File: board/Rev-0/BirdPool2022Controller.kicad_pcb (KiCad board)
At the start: 2 copper layers, 69.8 x 50.8 mm, 28 parts, among them J1 ISP, J2 OSTVN02A150, J3 OSTVN04A150, J4 OSTVN02A150, J5 OSTVN04A150, J6 Conn_01x06, K1 G5LE-14_DC5, U1 PC817, U2 PIC18F1330

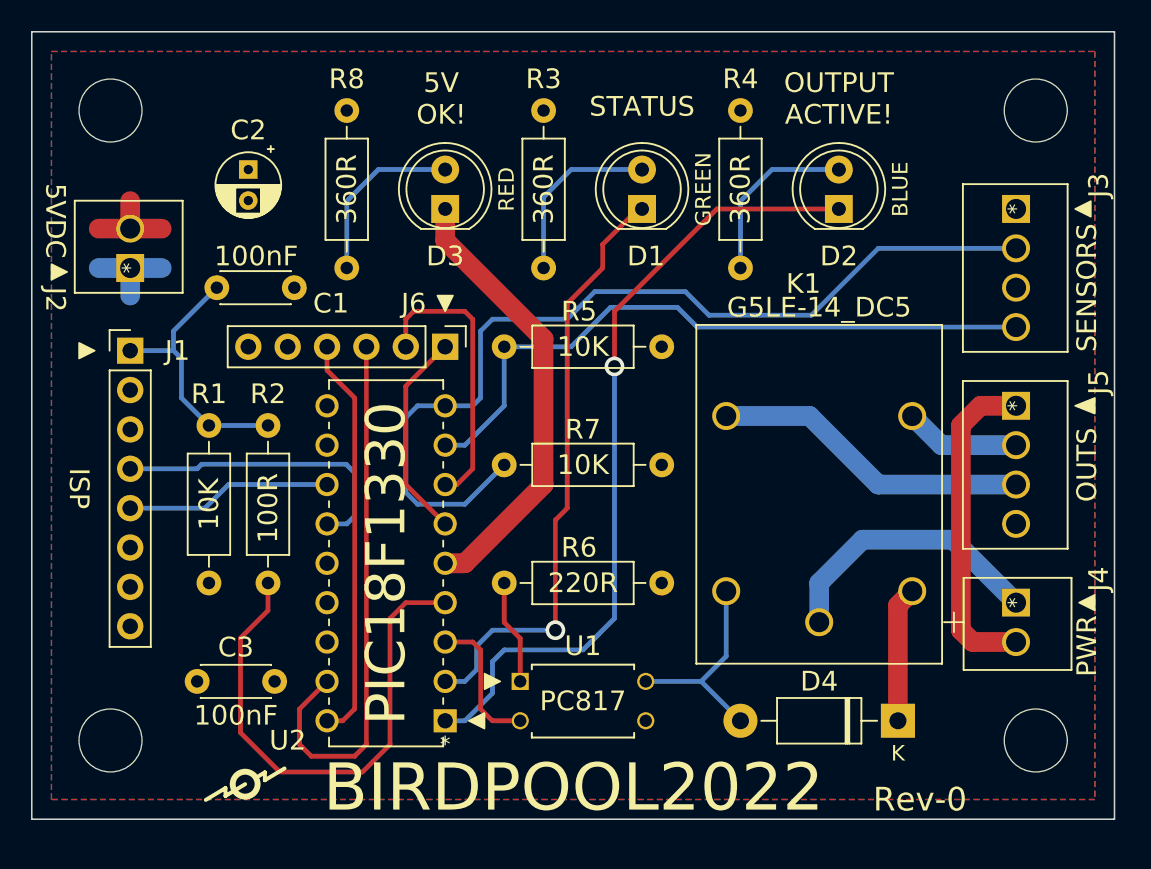
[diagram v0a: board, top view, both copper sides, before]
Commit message: UPD: Boards now with KiCad 6.0.0
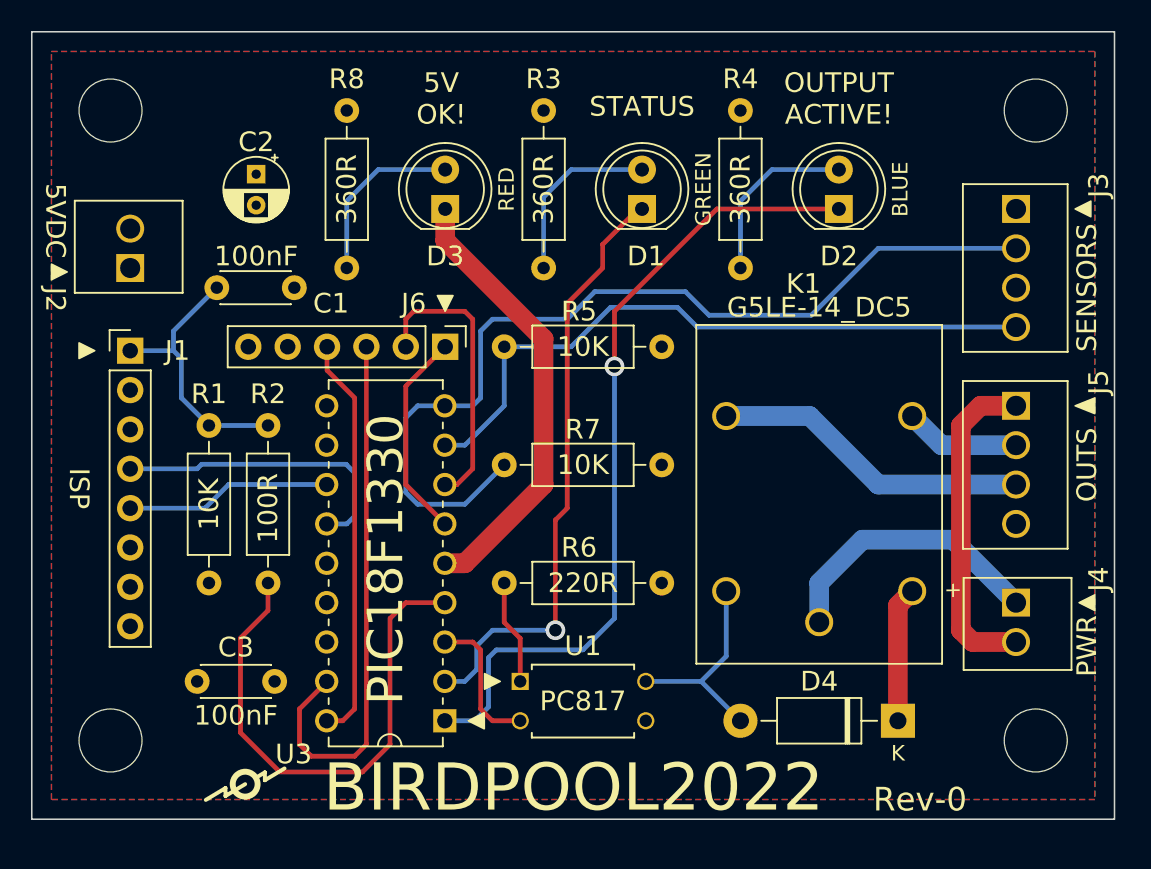
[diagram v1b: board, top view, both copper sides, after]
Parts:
- removed U2: PIC18F1330, My_Library:PDIP18_300MC_MCH
- added U3: PIC18F1330, My_Library:PDIP18_300MC_MCH, F.Cu at (107.9, 100.3)
- D4: value 4001 -> 1N4001
- moved C2 0.59 mm to (95.8, 65.1)
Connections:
- J1 pad 6: Net-(J1-Pad6) -> unconnected-(J1-Pad6)
- J1 pad 7: Net-(J1-Pad7) -> unconnected-(J1-Pad7)
- J1 pad 8: Net-(J1-Pad8) -> unconnected-(J1-Pad8)
- J5 pad 4: Net-(J5-Pad4) -> unconnected-(J5-Pad4)
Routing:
- net GND: track 34.7 -> 28.9 mm
- net +5V: track 14.8 -> 8.92 mm
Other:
- net class Default removed
